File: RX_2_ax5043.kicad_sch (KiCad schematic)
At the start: 17 parts, among them U305 AX5043, U307 TPS22929D

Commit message: Add a CPU thermsistor
Signed-off-by: Corey Minyard <corey@minyard.net>
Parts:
- C350: footprint Capacitor_SMD:C_0402_1005Metric -> Capacitor_SMD:C_0603_1608Metric_Pad1.08x0.95mm_HandSolder
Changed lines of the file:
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@@
 			)
 		)
-		(property "Footprint" "Capacitor_SMD:C_0402_1005Metric"
+		(property "Footprint" "Capacitor_SMD:C_0603_1608Metric_Pad1.08x0.95mm_HandSolder"
 			(at 299.4152 82.55 0)
 			(effects

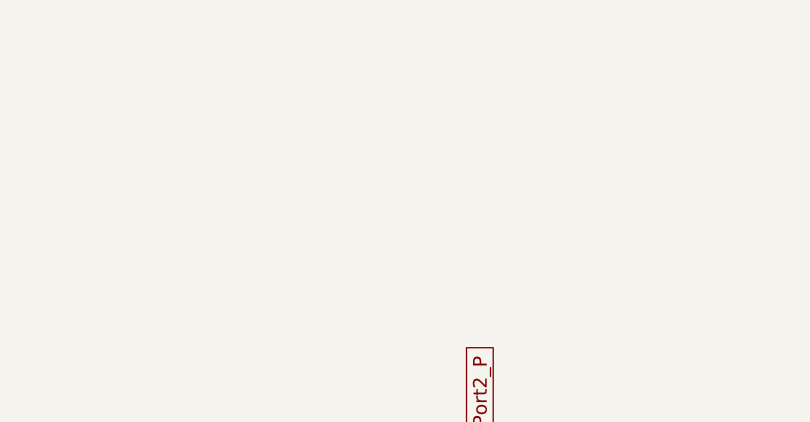
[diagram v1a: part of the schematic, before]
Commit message: Add shields around AX5043s, replace UFL connectors
Signed-off-by: Corey Minyard <corey@minyard.net>
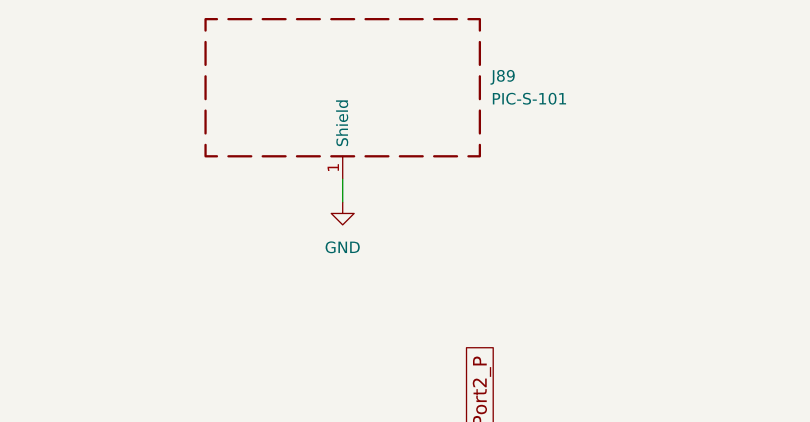
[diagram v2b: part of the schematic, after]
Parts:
- added J89: PIC-S-101, PacSatDev_misc:RF_SHIELD_PIC_S_101, symbol Device:RFShield_OnePiece
- P301: value ~ -> CONUFL001-SMD-T; footprint PacSatDev_misc:U_FL -> PacSatDev_misc:CONN1_CONUFL_TEC
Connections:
- net GND: now also J89.1 (Shield)
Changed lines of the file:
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@@
+	(wire
+		(pts
+			(xy 115.57 72.39) (xy 115.57 74.93)
+		)
+		(stroke
+			(width 0)
+			(type default)
+		)
+	)
 	(wire
 		(pts
@@
 			)
 		)
-		(property "Value" "~"
+		(property "Value" "CONUFL001-SMD-T"
 			(at 121.92 123.19 0)
 			(effects
@@
 					(size 1.27 1.27)
 				)
-			)
-		)
-		(property "Footprint" "PacSatDev_misc:U_FL"
+				(hide yes)
+			)
+		)
+		(property "Footprint" "PacSatDev_misc:CONN1_CONUFL_TEC"
 			(at 121.92 123.19 0)
 			(effects
@@
 				(path "/cc9f42d2-6985-41ac-acab-5ab7b01c5b38/1e7123c2-80dc-43cd-b90a-12f3fe1af0cb"
 					(reference "P301")
+					(unit 1)
+				)
+			)
+		)
+	)
+	(symbol
+		(lib_id "power:GND")
+		(at 115.57 74.93 0)
+		(unit 1)
+		(exclude_from_sim no)
+		(in_bom yes)
+		(on_board yes)
+		(dnp no)
+		(fields_autoplaced yes)
+		(property "Reference" "#PWR0193"
+			(at 115.57 81.28 0)
+			(effects
+				(font
+					(size 1.27 1.27)
+				)
+				(hide yes)
+			)
+		)
+		(property "Value" "GND"
+			(at 115.57 80.01 0)
+			(effects
+				(font
+					(size 1.27 1.27)
+				)
+			)
+		)
+		(property "Footprint" ""
+			(at 115.57 74.93 0)
+			(effects
+				(font
+					(size 1.27 1.27)
+				)
+				(hide yes)
+			)
+		)
+		(property "Datasheet" ""
+			(at 115.57 74.93 0)
+			(effects
+				(font
+					(size 1.27 1.27)
+				)
+				(hide yes)
+			)
+		)
+		(property "Description" ""
+			(at 115.57 74.93 0)
+			(effects
+				(font
+					(size 1.27 1.27)
+				)
+			)
+		)
+		(pin "1"
+		)
+		(instances
+			(project "PacSat_AFSK"
+				(path "/cc9f42d2-6985-41ac-acab-5ab7b01c5b38/1e7123c2-80dc-43cd-b90a-12f3fe1af0cb"
+					(reference "#PWR0193")
 					(unit 1)
 				)
@@
 					(unit 1)
 				)
+			)
+		)
+	)
+	(symbol
+		(lib_id "Device:RFShield_OnePiece")
+		(at 115.57 62.23 0)
+		(unit 1)
+		(exclude_from_sim no)
+		(in_bom yes)
+		(on_board yes)
+		(dnp no)
+		(fields_autoplaced yes)
+		(property "Reference" "J89"
+			(at 132.08 60.9599 0)
+			(effects
+				(font
+					(size 1.27 1.27)
+				)
+				(justify left)
+			)
+		)
+		(property "Value" "PIC-S-101"
+			(at 132.08 63.4999 0)
+			(effects
+				(font
+					(size 1.27 1.27)
+				)
+				(justify left)
+			)
+		)
+		(property "Footprint" "PacSatDev_misc:RF_SHIELD_PIC_S_101"
+			(at 115.57 64.77 0)
+			(effects
+				(font
+					(size 1.27 1.27)
+				)
+				(hide yes)
+			)
+		)
+		(property "Datasheet" "~"
+			(at 115.57 64.77 0)
+			(effects
+				(font
+					(size 1.27 1.27)
+				)
+				(hide yes)
+			)
+		)
+		(property "Description" "One-piece EMI RF shielding cabinet"
+			(at 115.57 62.23 0)
+			(effects
+				(font
+					(size 1.27 1.27)
+				)
+				(hide yes)
+			)
+		)
+		(pin "1"
+		)
+		(instances
+			(project "PacSat_AFSK"
+				(path "/cc9f42d2-6985-41ac-acab-5ab7b01c5b38/1e7123c2-80dc-43cd-b90a-12f3fe1af0cb"
+					(reference "J89")
+					(unit 1)
+				)

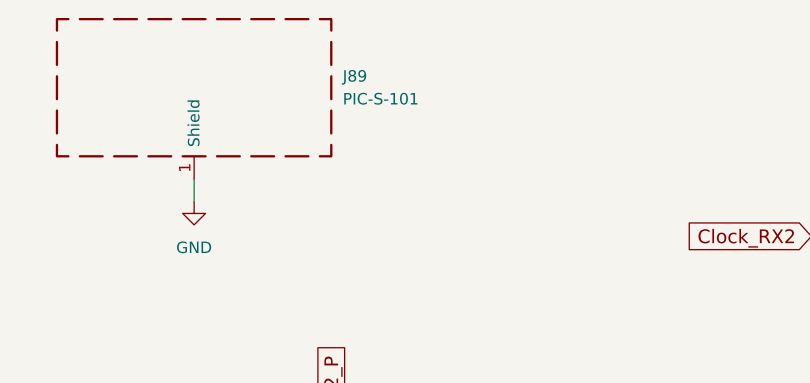
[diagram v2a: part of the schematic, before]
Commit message: More messing with RF shields
Signed-off-by: Corey Minyard <corey@minyard.net>
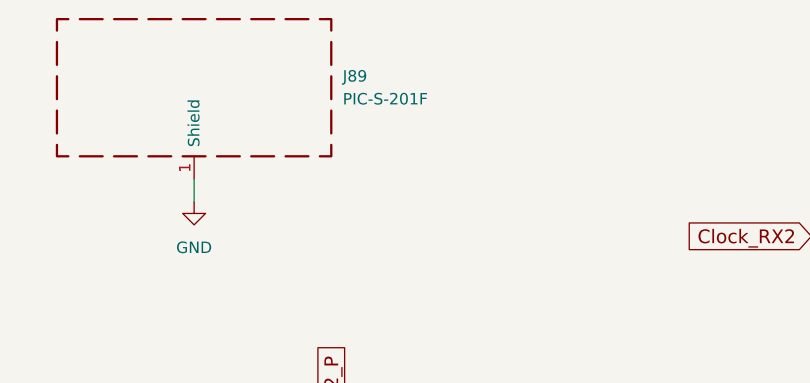
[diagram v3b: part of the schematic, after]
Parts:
- J89: value PIC-S-101 -> PIC-S-201F
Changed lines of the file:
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@@
 			)
 		)
-		(property "Value" "PIC-S-101"
+		(property "Value" "PIC-S-201F"
 			(at 132.08 63.4999 0)
 			(effects

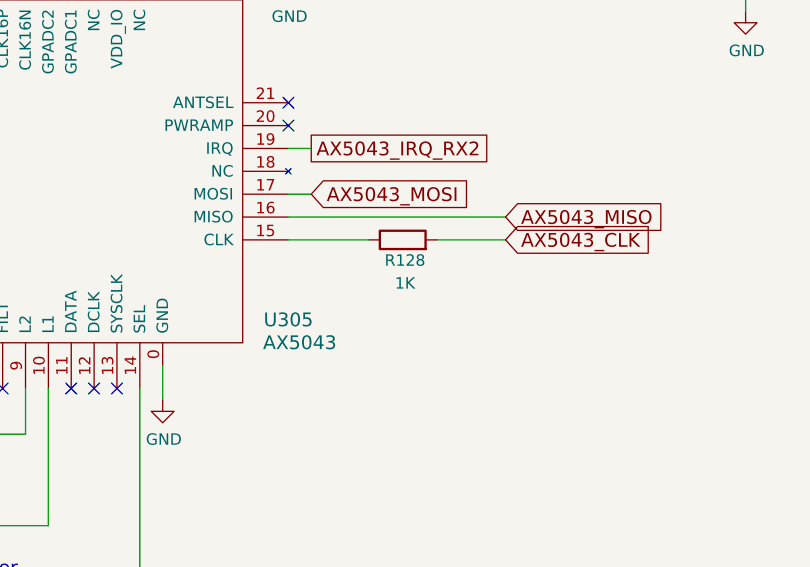
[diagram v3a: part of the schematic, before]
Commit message: Update SPI clock with simulation
Simulated the SPI clocks, updated resistor values based on findings.

Signed-off-by: Corey Minyard <corey@minyard.net>
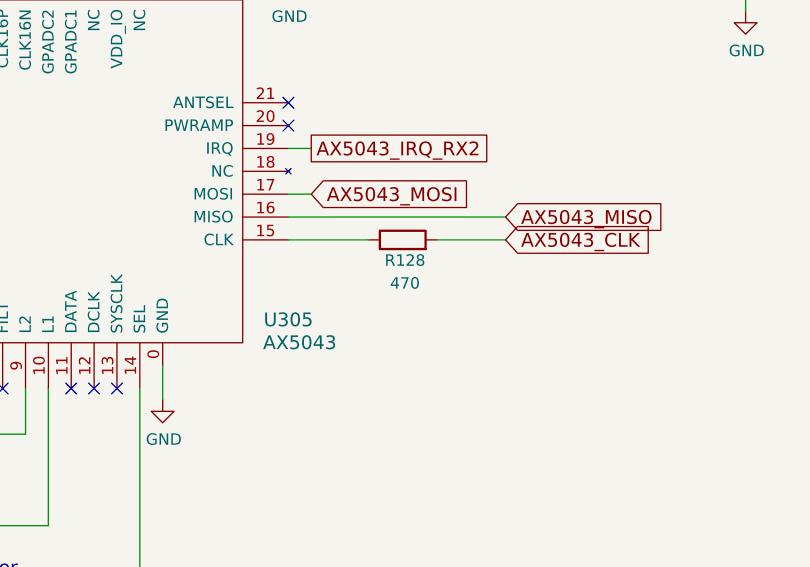
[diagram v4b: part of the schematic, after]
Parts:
- R128: value 1K -> 470
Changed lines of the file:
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@@
 			)
 		)
-		(property "Value" "1K"
+		(property "Value" "470"
 			(at 255.524 141.986 90)
 			(effects

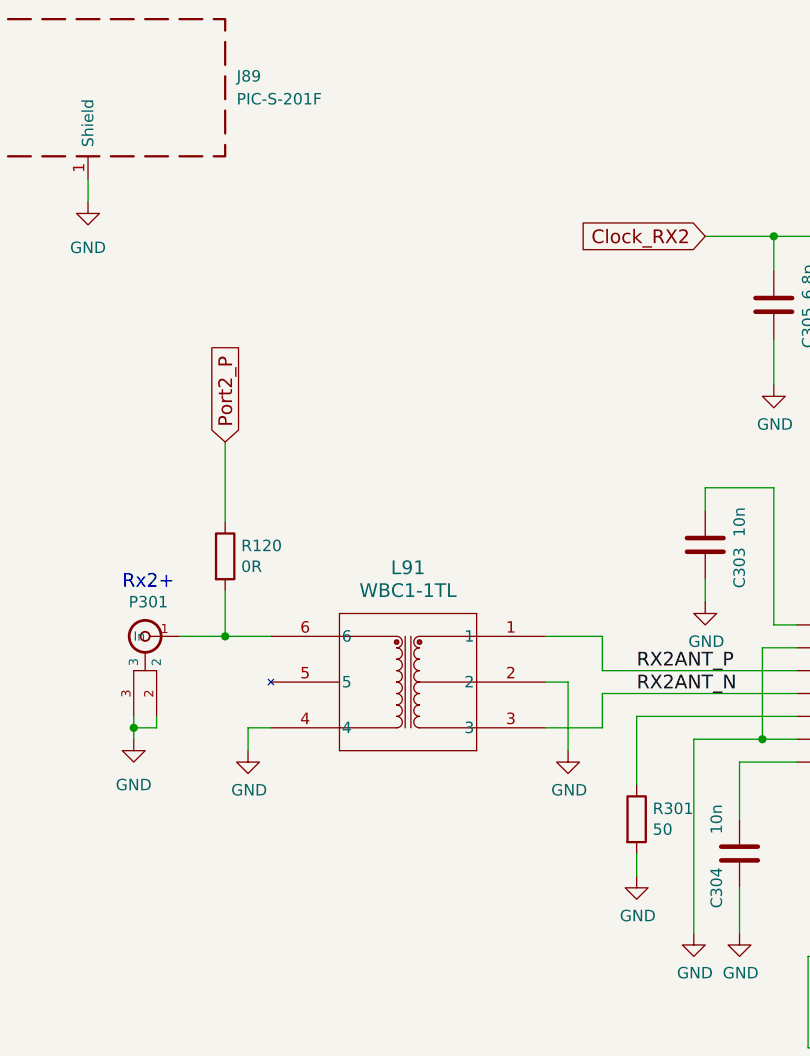
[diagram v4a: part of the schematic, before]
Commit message: Rework the AX5043 RX side to a different balun
It's cheaper (though not smaller) and fits inside the shield.

Signed-off-by: Corey Minyard <corey@minyard.net>
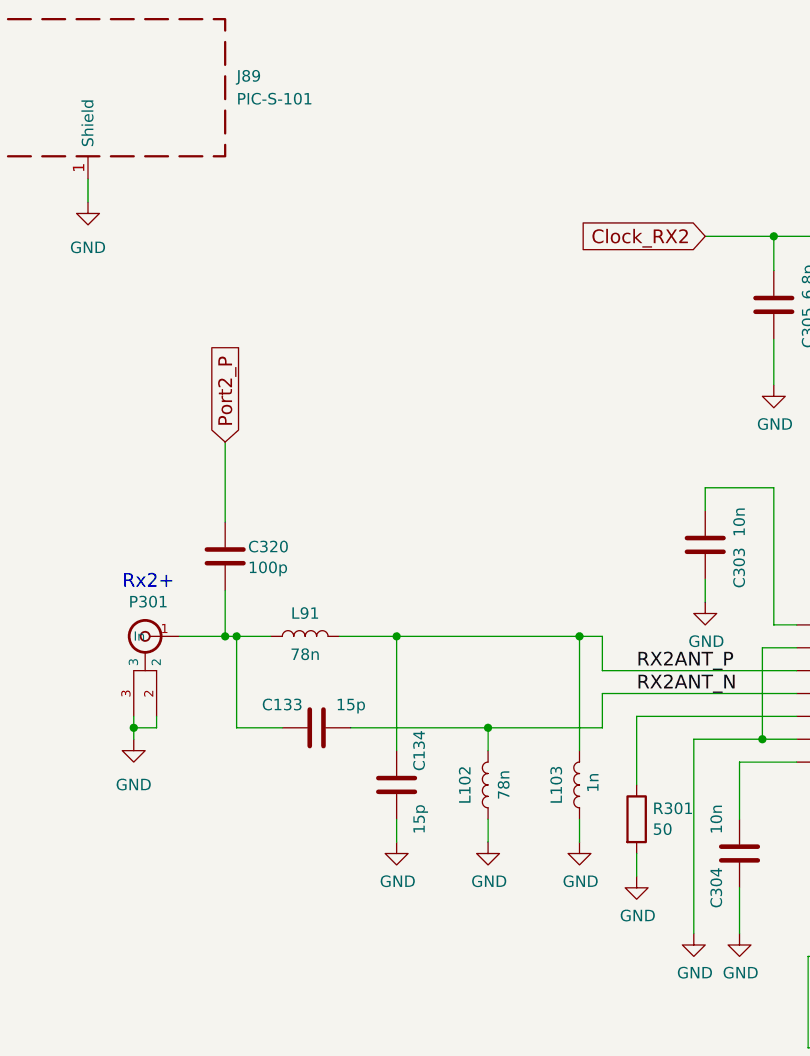
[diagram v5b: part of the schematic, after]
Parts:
- removed L91: WBC1-1TL, PacSatDev_misc:IND6_WBC1, symbol PACSAT_DEV_misc:WBC1-1TL
- added C133, C134: 15p, Capacitor_SMD:C_0603_1608Metric_Pad1.08x0.95mm_HandSolder, symbol Device:C
- added L102, L91: 78n, Inductor_SMD:L_0603_1608Metric_Pad1.05x0.95mm_HandSolder, symbol Device:L
- added L103: 1n, Inductor_SMD:L_0603_1608Metric_Pad1.05x0.95mm_HandSolder, symbol Device:L
- C320: renamed from R120; value 0R -> 100p; symbol Device:R -> Device:C
- J89: value PIC-S-201F -> PIC-S-101
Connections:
- net GND: now also C134.1, L102.1, L103.1
- net RX2ANT_N: now also C133.1, L102.2
- net RX2ANT_P: now also C134.2, L103.2, L91.2
- net at C320.2, P301.1 (In): now also C133.2, L91.1

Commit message: Change the AX5043 shield to a frame/cover setup
Easier access to parts underneath.

Signed-off-by: Corey Minyard <corey@minyard.net>
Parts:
- J89: value PIC-S-101 -> PIC-S-201F
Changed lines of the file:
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@@
 			)
 		)
-		(property "Value" "PIC-S-101"
+		(property "Value" "PIC-S-201F"
 			(at 132.08 63.4999 0)
 			(effects

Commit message: Re-annotate all parts
And get rid of the per-sheet annotation remarks.

Signed-off-by: Corey Minyard <corey@minyard.net>
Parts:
- renumbered C320 to C49, C133 to C50, C134 to C51, C303 to C52, C304 to C53, C305 to C54, C306 to C55, C307 to C56, C350 to C57, J89 to J3, L91 to L3, L102 to L4, L103 to L5, L301 to L6, P301 to P2, R301 to R52, R302 to R53, R303 to R54, R128 to R55, R92 to R56, U305 to U15, U307 to U16
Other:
- note removed: "Symbol Numbers 300 up"
